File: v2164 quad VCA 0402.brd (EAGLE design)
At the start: 39.4 x 14.6 mm, 44 parts, among them IC1 TL072JD, IC2 TL072JD

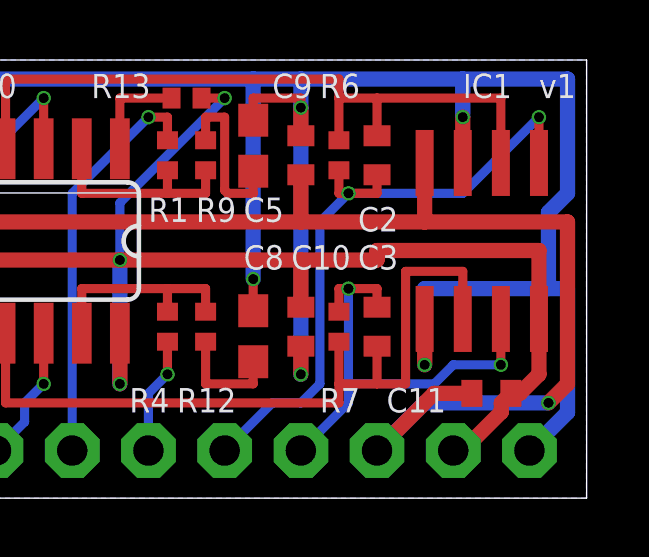
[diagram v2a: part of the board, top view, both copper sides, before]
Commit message: Added optional shottky diodes
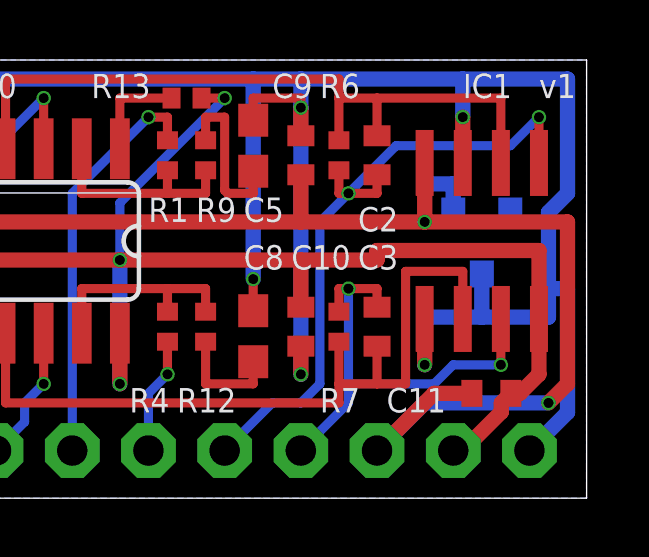
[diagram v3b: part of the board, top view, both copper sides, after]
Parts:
- added Q1: BA854SW, joakim:SOT23-3J
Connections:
- net -15V: now also Q1.1
- net GND: now also Q1.3
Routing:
- net -15V: track 67.0 -> 70.1 mm, vias 3 -> 4
- net GND: track 105.4 -> 106.9 mm
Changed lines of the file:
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@@
 <grid distance="12.5" unitdist="mil" unit="mil" style="lines" multiple="1" display="yes" altdistance="5" altunitdist="mil" altunit="mil"/>
 <layers>
-<layer number="1" name="Top" color="4" fill="1" visible="yes" active="yes"/>
+<layer number="1" name="Top" color="4" fill="1" visible="no" active="yes"/>
 <layer number="2" name="Route2" color="16" fill="1" visible="no" active="no"/>
 <layer number="15" name="Route15" color="23" fill="1" visible="no" active="no"/>
@@
 <layer number="19" name="Unrouted" color="6" fill="1" visible="yes" active="yes"/>
 <layer number="20" name="Dimension" color="24" fill="1" visible="yes" active="yes"/>
-<layer number="21" name="tPlace" color="7" fill="1" visible="yes" active="yes"/>
+<layer number="21" name="tPlace" color="7" fill="1" visible="no" active="yes"/>
 <layer number="22" name="bPlace" color="7" fill="1" visible="yes" active="yes"/>
-<layer number="23" name="tOrigins" color="15" fill="1" visible="yes" active="yes"/>
+<layer number="23" name="tOrigins" color="15" fill="1" visible="no" active="yes"/>
 <layer number="24" name="bOrigins" color="15" fill="1" visible="yes" active="yes"/>
-<layer number="25" name="tNames" color="7" fill="1" visible="yes" active="yes"/>
+<layer number="25" name="tNames" color="7" fill="1" visible="no" active="yes"/>
 <layer number="26" name="bNames" color="7" fill="1" visible="yes" active="yes"/>
 <layer number="27" name="tValues" color="7" fill="1" visible="no" active="yes"/>
@@
 <layer number="37" name="tTest" color="7" fill="1" visible="no" active="yes"/>
 <layer number="38" name="bTest" color="7" fill="1" visible="no" active="yes"/>
-<layer number="39" name="tKeepout" color="4" fill="11" visible="yes" active="yes"/>
+<layer number="39" name="tKeepout" color="4" fill="11" visible="no" active="yes"/>
 <layer number="40" name="bKeepout" color="1" fill="11" visible="yes" active="yes"/>
-<layer number="41" name="tRestrict" color="4" fill="10" visible="yes" active="yes"/>
+<layer number="41" name="tRestrict" color="4" fill="10" visible="no" active="yes"/>
 <layer number="42" name="bRestrict" color="1" fill="10" visible="yes" active="yes"/>
 <layer number="43" name="vRestrict" color="2" fill="10" visible="no" active="yes"/>
@@
 <layer number="49" name="Reference" color="7" fill="1" visible="no" active="yes"/>
 <layer number="50" name="dxf" color="7" fill="1" visible="no" active="no"/>
-<layer number="51" name="tDocu" color="7" fill="1" visible="yes" active="yes"/>
+<layer number="51" name="tDocu" color="7" fill="1" visible="no" active="yes"/>
 <layer number="52" name="bDocu" color="7" fill="1" visible="yes" active="yes"/>
 <layer number="53" name="tGND_GNDA" color="7" fill="9" visible="no" active="no"/>
@@
 </element>
 <element name="U$1" library="joakim" package="XONIK_LOGO_20" value="" x="29.845" y="8.255" smashed="yes" rot="MR0"/>
+<element name="Q1" library="joakim" package="SOT23-3J" value="BA854SW" x="35.8775" y="8.5725" smashed="yes" rot="MR180">
+<attribute name="VALUE" x="34.8615" y="8.763" size="0.4064" layer="28" rot="MR180"/>
+</element>
 </elements>
 <signals>
@@
 <wire x1="33.9725" y1="5.9725" x2="33.9725" y2="4.445" width="0.508" layer="1"/>
 <via x="33.9725" y="4.445" extent="1-16" drill="0.3302"/>
-<wire x1="38.1" y1="6.985" x2="33.9725" y2="6.985" width="0.508" layer="16"/>
+<wire x1="38.1" y1="6.0325" x2="35.8775" y2="6.0325" width="0.508" layer="16"/>
+<wire x1="35.8775" y1="6.0325" x2="33.9725" y2="6.0325" width="0.508" layer="16"/>
 <wire x1="38.1" y1="9.525" x2="38.735" y2="10.16" width="0.508" layer="16"/>
 <wire x1="38.735" y1="10.16" x2="38.735" y2="13.97" width="0.508" layer="16"/>
+<wire x1="38.1" y1="6.0325" x2="38.1" y2="6.985" width="0.508" layer="16"/>
 <wire x1="38.1" y1="6.985" x2="38.1" y2="9.525" width="0.508" layer="16"/>
 <via x="2.2225" y="13.0175" extent="1-16" drill="0.3302"/>
@@
 <wire x1="38.735" y1="2.8575" x2="38.735" y2="6.985" width="0.508" layer="16"/>
 <wire x1="38.735" y1="6.985" x2="38.1" y2="6.985" width="0.508" layer="16"/>
-<wire x1="33.9725" y1="6.985" x2="33.9725" y2="4.445" width="0.508" layer="16"/>
+<wire x1="33.9725" y1="6.0325" x2="33.9725" y2="4.445" width="0.508" layer="16"/>
+<contactref element="Q1" pad="3"/>
+<wire x1="35.8775" y1="7.4725" x2="35.8775" y2="6.0325" width="0.508" layer="16"/>
 </signal>
 <signal name="N$1">
@@
 <wire x1="38.735" y1="9.2075" x2="33.9725" y2="9.2075" width="0.508" layer="1"/>
 <wire x1="33.9725" y1="3.175" x2="32.385" y2="1.5875" width="0.508" layer="16"/>
+<contactref element="Q1" pad="1"/>
+<wire x1="34.9275" y1="9.5725" x2="34.925" y2="9.575" width="0.508" layer="16"/>
+<wire x1="34.925" y1="9.575" x2="34.925" y2="10.4775" width="0.508" layer="16"/>
+<wire x1="34.925" y1="10.4775" x2="33.9725" y2="10.4775" width="0.508" layer="16"/>
+<wire x1="33.9725" y1="10.4775" x2="33.9725" y2="9.2075" width="0.508" layer="16"/>
+<via x="33.9725" y="9.2075" extent="1-16" drill="0.3302"/>
 </signal>
 <signal name="OUT4">
@@
 <wire x1="37.7825" y1="11.1725" x2="37.7825" y2="12.7" width="0.3048" layer="1"/>
 <via x="37.7825" y="12.7" extent="1-16" drill="0.3302"/>
-<wire x1="37.7825" y1="12.7" x2="35.2425" y2="10.16" width="0.3048" layer="16"/>
-<wire x1="35.2425" y1="10.16" x2="31.4325" y2="10.16" width="0.3048" layer="16"/>
+<wire x1="37.7825" y1="12.7" x2="36.83" y2="11.7475" width="0.3048" layer="16"/>
+<wire x1="36.83" y1="11.7475" x2="33.02" y2="11.7475" width="0.3048" layer="16"/>
+<wire x1="33.02" y1="11.7475" x2="31.4325" y2="10.16" width="0.3048" layer="16"/>
 <via x="31.4325" y="10.16" extent="1-16" drill="0.3302"/>
 <wire x1="31.4325" y1="10.16" x2="32.385" y2="10.16" width="0.3048" layer="1"/>
